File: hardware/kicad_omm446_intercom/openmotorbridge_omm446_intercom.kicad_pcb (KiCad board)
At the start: 4 copper layers, 60 x 30 mm, 20 parts, among them J1 TYPE-C-31-M-12_IP67, J2 J_AUDIO_PWR, SW1 BTN_PTT, SW2 BTN_MODE, SW3 BTN_CH_UP, SW4 BTN_CH_DOWN, U1 ESP32-C6-MINI-1U, U2 BQ24075RGTR, U3 SA818-DMR, U4 ES8388, U5 ME6211C33M5G

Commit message: fix(hw): add 3D model for NiceRF SA818-DMR and connectors, correct orientation and routing for PCBA 10
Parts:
- moved U3 5.39 mm to (100.0, 103.0)
- moved J_RF 5.00 mm to (122.5, 95.0)
- moved PAD_ANT 2.00 mm to (126.0, 95.0)
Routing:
- net VCC_3V3: track 66.7 -> 32.1 mm
- net CHG_STAT: track 27.7 -> 9.05 mm
- net USB_DP: track 40.1 -> 22.2 mm
- net BTN_PTT: track 35.0 -> 23.5 mm
- net I2S_DOUT: track 20.2 -> 9.72 mm
- net BTN_MODE: track 12.0 -> 3.21 mm
- net WS2812_DATA: track 9.80 -> 1.34 mm
- net GND: track 112.9 -> 104.7 mm
- net I2C_SCL: track 22.4 -> 14.2 mm
- net RF_ANT: track 23.8 -> 15.8 mm
- net USB_DN: track 33.1 -> 26.2 mm
- net VBUS_5V: track 56.8 -> 51.2 mm
- net I2S_WS: track 19.5 -> 14.1 mm
- net SYS_PWR: track 11.4 -> 6.63 mm
- net I2S_DIN: track 20.2 -> 15.7 mm
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
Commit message: fix(hw): remove incorrect J2 connector from PCBA 10 (UCS modules interface via USB-C)
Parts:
- removed J2: J_AUDIO_PWR, JST_SH_BM08B-SRSS-TB_1x08-1MP_P1.00mm_Vertical
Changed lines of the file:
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@@
-		)
-	)
-	(footprint "JST_SH_BM08B-SRSS-TB_1x08-1MP_P1.00mm_Vertical"
-		(layer "B.Cu")
-		(at 88 88 180)
-		(descr "JST SH series 8-Pin 1.0mm vertical connector BM08B-SRSS-TB (Kelvin Docking)")
-		(tags "connector JST SH vertical 8pin")
-		(property "Reference" "J2"
-			(at 0 -2.5 180)
-			(layer "B.SilkS")
-			(effects (font (size 0.9 0.9) (thickness 0.12)) (justify mirror))
-		)
-		(property "Value" "J_AUDIO_PWR"
-			(at 0 2.5 180)
-			(layer "B.Fab")
-			(effects (font (size 0.9 0.9) (thickness 0.12)) (justify mirror))
-		)
-		(attr smd)
-		(pad "1" smd roundrect (at -3.5 0 180) (size 0.6 1.55) (layers "B.Cu" "B.Paste" "B.Mask") (roundrect_rratio 0.25) (net "PGND"))
-		(pad "2" smd roundrect (at -2.5 0 180) (size 0.6 1.55) (layers "B.Cu" "B.Paste" "B.Mask") (roundrect_rratio 0.25) (net "VBUS_5V"))
-		(pad "3" smd roundrect (at -1.5 0 180) (size 0.6 1.55) (layers "B.Cu" "B.Paste" "B.Mask") (roundrect_rratio 0.25) (net "AGND_SPK"))
-		(pad "4" smd roundrect (at -0.5 0 180) (size 0.6 1.55) (layers "B.Cu" "B.Paste" "B.Mask") (roundrect_rratio 0.25) (net "HP_OUT_L"))
-		(pad "5" smd roundrect (at 0.5 0 180) (size 0.6 1.55) (layers "B.Cu" "B.Paste" "B.Mask") (roundrect_rratio 0.25) (net "HP_OUT_R"))
-		(pad "6" smd roundrect (at 1.5 0 180) (size 0.6 1.55) (layers "B.Cu" "B.Paste" "B.Mask") (roundrect_rratio 0.25) (net "AGND_MIC"))
-		(pad "7" smd roundrect (at 2.5 0 180) (size 0.6 1.55) (layers "B.Cu" "B.Paste" "B.Mask") (roundrect_rratio 0.25) (net "MIC_IN+"))
-		(pad "8" smd roundrect (at 3.5 0 180) (size 0.6 1.55) (layers "B.Cu" "B.Paste" "B.Mask") (roundrect_rratio 0.25) (net "PTT_IO"))
-		(pad "MP1" smd roundrect (at -4.8 1.8 180) (size 1.2 1.8) (layers "B.Cu" "B.Paste" "B.Mask") (roundrect_rratio 0.25) (net "PGND"))
-		(pad "MP2" smd roundrect (at 4.8 1.8 180) (size 1.2 1.8) (layers "B.Cu" "B.Paste" "B.Mask") (roundrect_rratio 0.25) (net "PGND"))
-		(model "${KICAD10_3DMODEL_DIR}/Connector_JST.3dshapes/JST_SH_BM08B-SRSS-TB_1x08-1MP_P1.00mm_Vertical.step"
-			(offset (xyz 0 0 0))
-			(scale (xyz 1 1 1))
-			(rotate (xyz 0 0 0))
 		)
 	)

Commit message: feat(hw): finalize PCBA 10 OMM 446 routing, schematic parity, 3D renders, and JLCPCB packages
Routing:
- net GND: track 104.7 -> 226.6 mm, vias 15 -> 21
- net VCC_3V3: track 32.1 -> 60.7 mm, vias 9 -> 10
- net USB_DP: track 22.2 -> 45.5 mm, vias 8 -> 9
- net RF_ANT: track 15.8 -> 34.4 mm, vias 1 -> 5
- net CHG_STAT: track 9.05 -> 26.5 mm, vias 4 -> 6
- net USB_DN: track 26.2 -> 38.8 mm
- net I2C_SCL: track 14.2 -> 26.5 mm, vias 2 -> 0
- net I2S_DOUT: track 9.72 -> 21.8 mm
- net VBUS_5V: track 51.2 -> 62.4 mm, vias 4 -> 0
- net WS2812_DATA: track 1.34 -> 12.1 mm, vias 2 -> 4
- net BTN_MODE: track 3.21 -> 13.3 mm
- net SYS_PWR: track 6.63 -> 16.4 mm, vias 2 -> 5
- net AGND_SPK: track 62.3 -> 68.7 mm, vias 5 -> 4
- net HP_OUT_L: track 58.5 -> 64.9 mm, vias 2 -> 4
- net BTN_PTT: track 23.5 -> 29.7 mm, vias 2 -> 4
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
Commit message: feat(hw,docs): implement Dual-Engine OMB Lite architecture for PCBA 09 and PCBA 10
- Schematic: Add ESP32-PICO-V3-02 (BT Classic/BLE co-processor) and Johanson 2450AT18 chip antenna
- PCB: Add Grobplatzierung and Vorverbindung nets on B.Cu for PCBA 09 and PCBA 10
- Firmware: Add co-processor UART link config and disable BT on C6 to eliminate CoEx time-slicing
- Documentation: Add Dual-Engine architecture, Cardo DMC Bridge / Sena Bridge, and Profile C OMB Lite
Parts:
- added ANT1: 2.45GHz_Chip_Antenna, RF_Antenna:Johanson_2450AT18x100, B.Cu at (78.0, 88.0)
- added U6: ESP32-PICO-V3-02, Package_DFN_QFN:QFN-48-1EP_7x7mm_P0.5mm_EP5.3x5.3mm, B.Cu at (88.0, 92.0)

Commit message: feat(hw): finalize DRC, 3D renders, and production packages for PCBA 09 and PCBA 10
- PCBA 09 (OMM 2.4 GHz Intercom & UCS): 0 unconnected items, 0 electrical errors
- PCBA 10 (OMM 446 MHz PMR/DMR Transceiver): 0 unconnected items, 0 electrical errors
- Updated high-resolution 3D renders (top, bottom, and isometric views)
- Regenerated JLCPCB manufacturing packages (Gerbers, Drill, BOM, CPL) with ESP32-PICO-V3-02 (C2686884) and Johanson 2450AT18x100 antenna (C2909988)
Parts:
- moved U4 38.2 mm to (88.9, 110.5)
- moved J_RF 6.32 mm to (126.0, 100.2)
- moved PAD_ANT 5.25 mm to (126.0, 100.2)
- moved U2 5.03 mm to (116.2, 94.5)
- moved U6 3.36 mm to (85.5, 89.8)
- moved ANT1 1.77 mm to (78.2, 86.2)
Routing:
- net GND: track 226.6 -> 141.7 mm, vias 21 -> 16
- net AGND_SPK: track 68.7 -> 20.9 mm, vias 4 -> 2
- net HP_OUT_R: track 62.6 -> 18.1 mm, vias 6 -> 0
- net HP_OUT_L: track 64.9 -> 21.4 mm, vias 4 -> 2
- net MIC_IN+: track 59.0 -> 21.1 mm, vias 4 -> 2
- net VCC_3V3: track 60.7 -> 91.8 mm, vias 10 -> 14
- net I2S_DOUT: track 21.8 -> 40.0 mm
- net I2S_WS: track 19.0 -> 35.1 mm, vias 2 -> 3
- net I2S_DIN: track 21.5 -> 36.4 mm
- net RF_ANT: track 34.4 -> 21.4 mm, vias 5 -> 2
- net VBUS_5V: track 62.4 -> 49.6 mm, vias 0 -> 4
- net I2S_BCLK: track 19.3 -> 31.2 mm, vias 0 -> 4
- net I2S_MCLK: track 17.1 -> 28.7 mm, vias 0 -> 4
- net BT_ANT: track 0.00 -> 9.41 mm, vias 0 -> 2
- net USB_DP: track 45.5 -> 36.4 mm, vias 9 -> 6
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
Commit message: feat(omm): set compact stubby antenna as helmet default, add internal J_HELMET audio & maintain external USB-C
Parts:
- added J_HELMET: HELMET_AUDIO_6P, JST_SH_SM06B-SRSS-TB_1x06-1MP_P1.00mm_Horizontal, B.Cu at (76.5, 104.0)

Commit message: feat: sync re-routed PCBAs (01, 03, 07, 08, 10), manufacturing packages, 3D renders & docs
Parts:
- moved J_HELMET 50.3 mm to (126.6, 99.8), turned to -90 degrees
- moved J_RF 20.4 mm to (110.5, 87.0), turned to 0 degrees
- moved PAD_ANT 20.4 mm to (110.5, 87.0)
- moved U5 13.4 mm to (114.2, 87.8), turned to -90 degrees
- moved U4 6.50 mm to (88.9, 104.0), turned to 180 degrees
- moved BAT1 4.88 mm to (120.5, 88.0)
- moved U2 1.82 mm to (117.2, 93.0), turned to 180 degrees
- moved ANT1 1.80 mm to (79.8, 87.2)
- moved U6 1.29 mm to (86.8, 89.5)
- turned U1 to 0 degrees
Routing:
- net GND: track 141.7 -> 36.8 mm, vias 16 -> 8
- net HP_OUT_L: track 21.4 -> 71.9 mm, vias 2 -> 6
- net MIC_IN+: track 21.1 -> 67.2 mm
- net BTN_PTT: track 24.5 -> 66.2 mm, vias 4 -> 7
- net AGND_SPK: track 20.9 -> 58.6 mm, vias 2 -> 4
- net HP_OUT_R: track 18.1 -> 53.1 mm, vias 0 -> 2
- net I2S_DOUT: track 40.0 -> 11.3 mm
- net I2S_WS: track 35.1 -> 11.0 mm, vias 3 -> 0
- net I2S_DIN: track 36.4 -> 13.0 mm
- net I2C_SDA: track 30.2 -> 7.19 mm, vias 4 -> 0
- net I2C_SCL: track 28.0 -> 6.10 mm, vias 4 -> 2
- net USB_DN: track 39.1 -> 18.5 mm, vias 4 -> 2
- net I2S_BCLK: track 31.2 -> 11.1 mm, vias 4 -> 2
- net I2S_MCLK: track 28.7 -> 9.21 mm, vias 4 -> 2
- net USB_DP: track 36.4 -> 20.0 mm, vias 6 -> 4
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
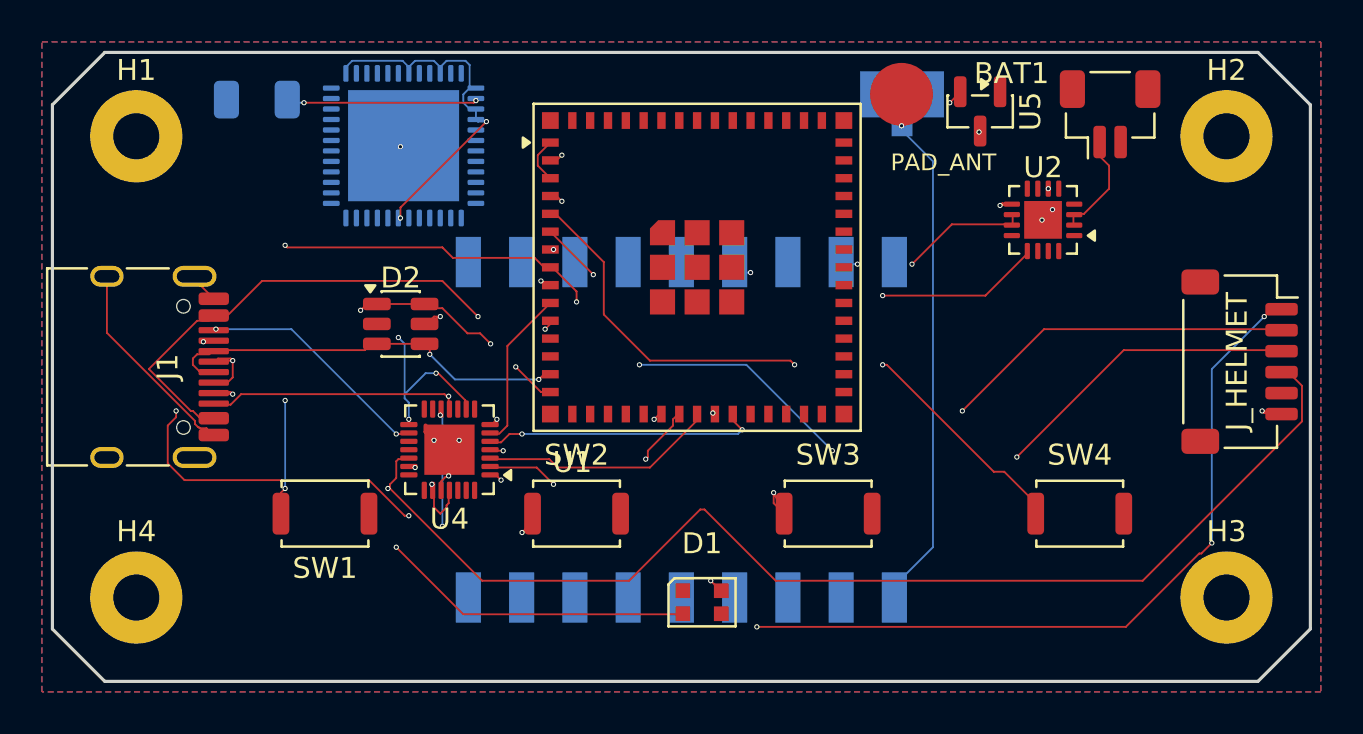
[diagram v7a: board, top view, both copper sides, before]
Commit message: hardware(omm): rotate J_HELMET by 180° inward, update CAD cutouts, CPL, gerbers, and docs
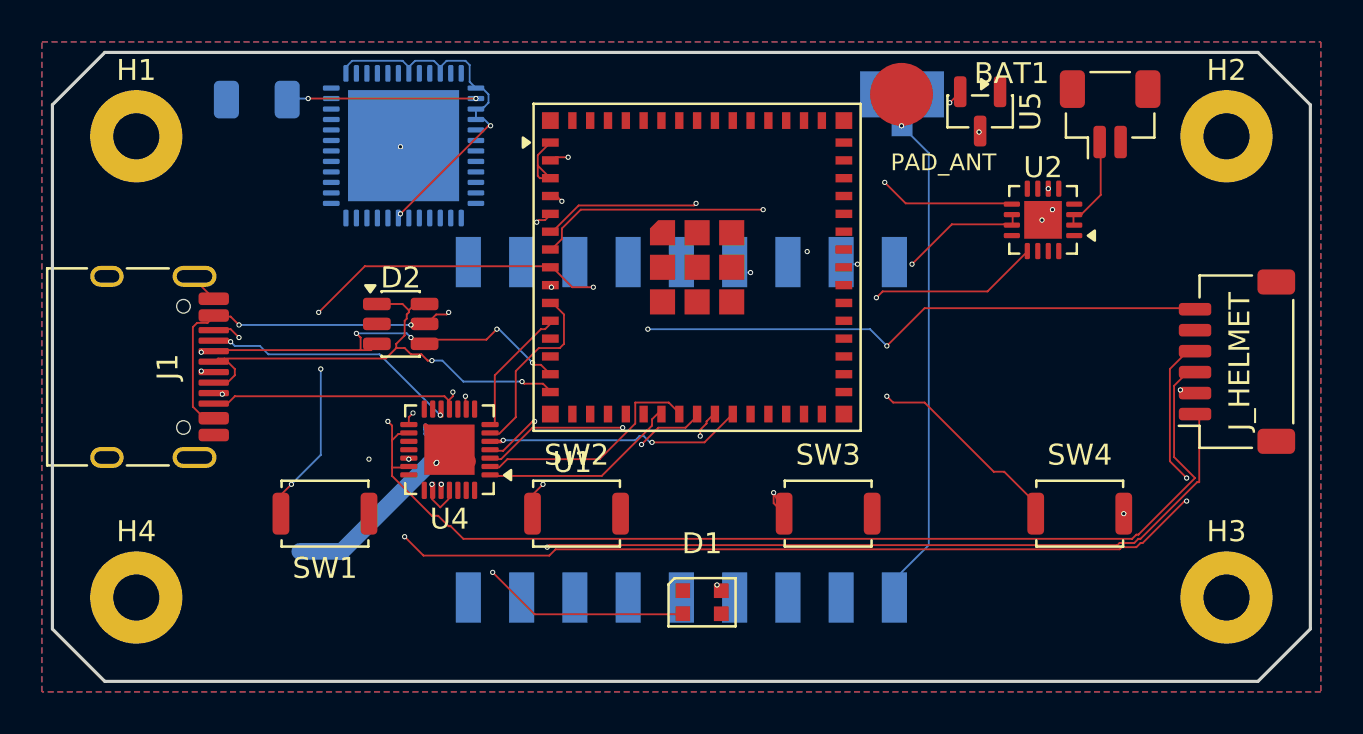
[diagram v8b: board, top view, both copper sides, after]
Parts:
- moved J_HELMET 0.12 mm to (126.5, 99.8), turned to 90 degrees
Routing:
- net VCC_3V3: track 80.3 -> 97.6 mm, vias 9 -> 8
- net HP_OUT_L: track 71.9 -> 56.1 mm, vias 6 -> 3
- net BTN_PTT: track 66.2 -> 54.3 mm, vias 7 -> 6
- net GND: track 36.8 -> 25.2 mm, vias 8 -> 7
- net WS2812_DATA: track 20.5 -> 30.6 mm
- net BTN_MODE: track 18.3 -> 10.3 mm
- net VBUS_5V: track 52.2 -> 45.9 mm, vias 3 -> 4
- net MIC_IN+: track 67.2 -> 61.2 mm, vias 2 -> 6
- net HP_OUT_R: track 53.1 -> 47.6 mm
- net USB_DP: track 20.0 -> 22.9 mm, vias 4 -> 2
- net BTN_CH_DOWN: track 30.1 -> 32.6 mm, vias 2 -> 3
- net AGND_SPK: track 58.6 -> 61.1 mm, vias 4 -> 2
- net USB_DN: track 18.5 -> 19.9 mm, vias 2 -> 6
- net I2C_SDA: track 7.19 -> 8.28 mm
- net I2S_DOUT: track 11.3 -> 12.4 mm
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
